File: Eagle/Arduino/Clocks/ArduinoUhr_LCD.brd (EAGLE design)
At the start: 100 x 80 mm, 13 parts

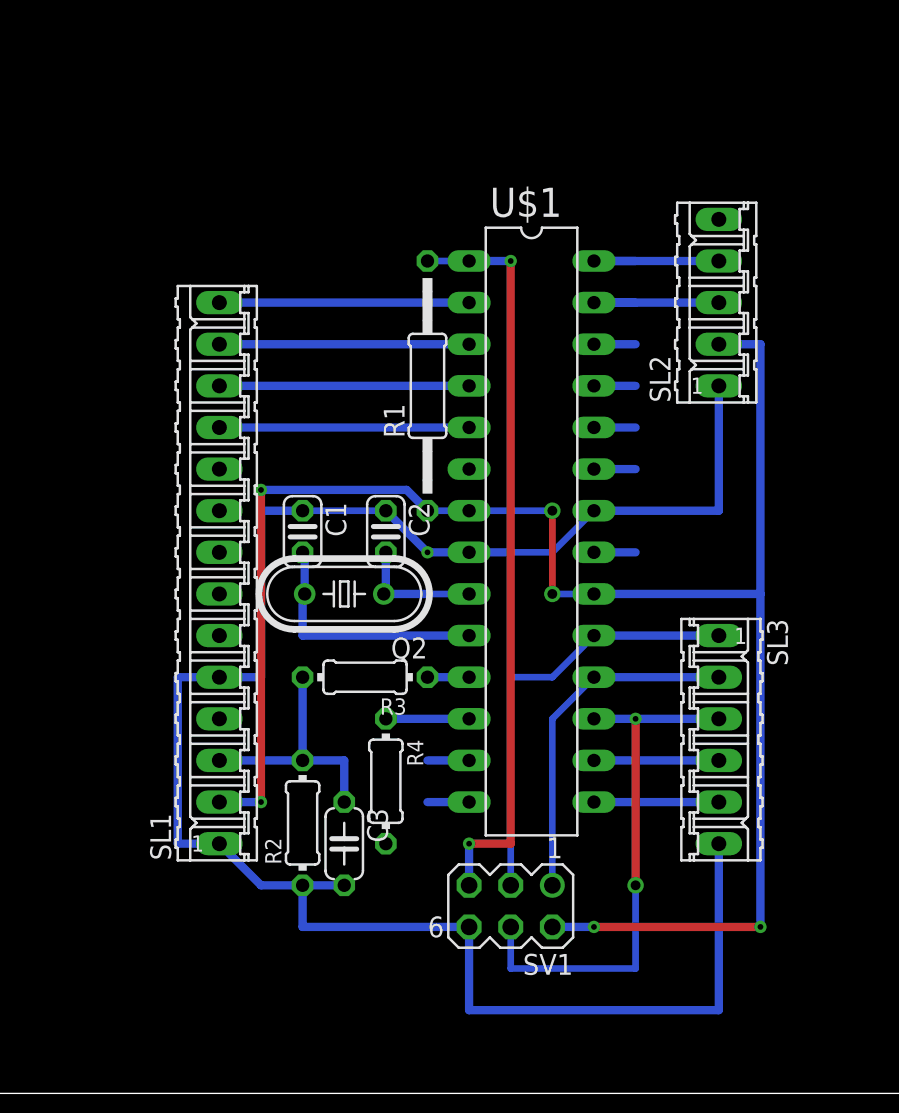
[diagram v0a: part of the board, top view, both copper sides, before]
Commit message: changed layout for new LCD Display
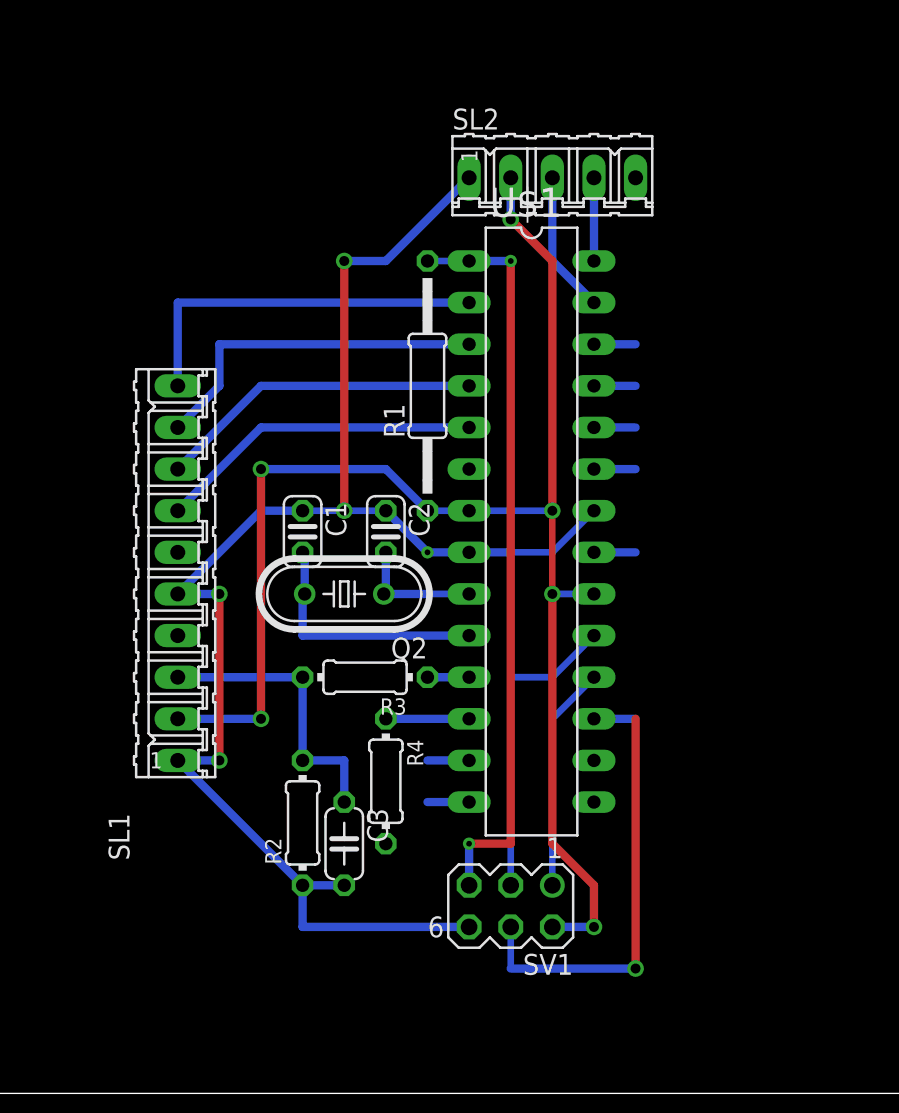
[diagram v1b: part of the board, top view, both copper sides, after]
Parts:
- removed SL3: (no value), con-amp-quick:06P
- SL1: device con-amp-quick:14P -> con-amp-quick:10P
- moved SL2 12.7 mm to (48.3, 55.9), turned to 0 degrees
- moved SL1 2.54 mm to (25.4, 31.8)
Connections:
- removed net D0: SL1.11, U$1.5
- removed net D1: SL1.12, U$1.4
- removed net D2: SL1.13, U$1.3
- removed net D3: SL1.14, U$1.2
- new net N$1: SL1.10, U$1.2
- new net N$2: SL1.9, U$1.3
- new net N$3: SL1.8, U$1.4
- new net N$4: SL1.7, U$1.5
- net DIO10(PWM): no longer SL3.4
- net DIO11(PWM)MOSI: no longer SL3.3
- net DIO12/MISO: no longer SL3.2
- net DIO9(PWM): no longer SL3.5
- net GND: no longer SL3.6
- net SCK[L5]: no longer SL3.1
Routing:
- net N$1: track 0.00 -> 22.9 mm
- net GND: track 117.5 -> 95.8 mm, vias 2 -> 6
- net N$2: track 0.00 -> 21.4 mm
- net N$4: track 0.00 -> 19.9 mm
- net N$3: track 0.00 -> 19.9 mm
- net VCC: track 108.5 -> 92.1 mm
- net D3: track 15.2 -> 0.00 mm
- net D2: track 15.2 -> 0.00 mm
- net D1: track 15.2 -> 0.00 mm
- net D0: track 15.2 -> 0.00 mm
- net SCK[L5]: track 26.5 -> 18.8 mm
- net DIO9(PWM): track 7.62 -> 0.00 mm
- net DIO12/MISO: track 21.4 -> 13.8 mm
- net DIO10(PWM): track 7.62 -> 0.00 mm
- net A5[SCL]: track 10.2 -> 5.08 mm
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
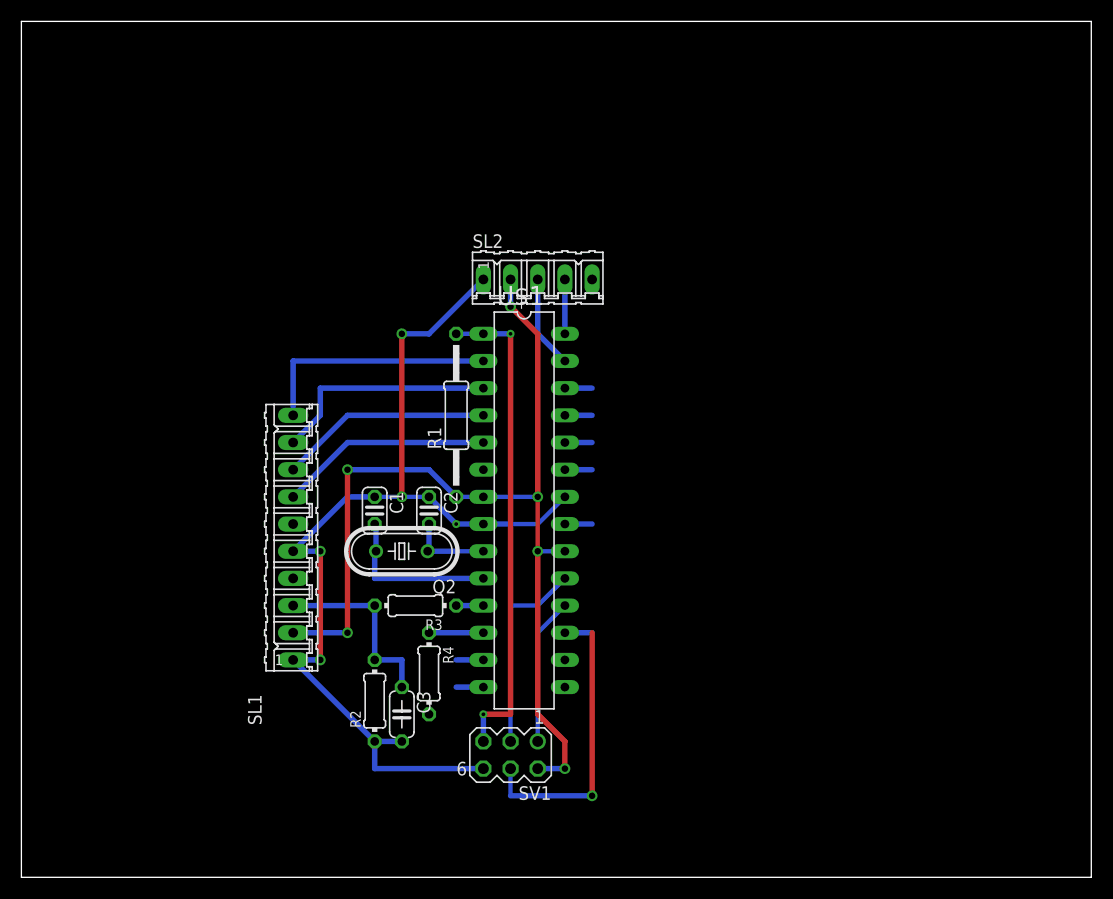
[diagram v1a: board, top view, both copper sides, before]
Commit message: Changes for severals files
bugfixes, pins changed
 - Arduino/Sketches/Uhren/ClockWithTimers/clockwithtimers/SettingStates.cpp
 - Arduino/Sketches/Uhren/ClockWithTimers/clockwithtimers/big_ben.h
 - Arduino/Sketches/Uhren/ClockWithTimers/clockwithtimers/clockwithtimers.ino
 - Arduino/Sketches/Uhren/ClockWithTimers/clockwithtimers/ioAt328.h
 - Arduino/Sketches/Uhren/ClockWithTimers/clockwithtimers/ioMega2560.h
bugfixes, and comments
 - Arduino/libraries/Melody/examples/melody_play/melody_play.ino
 - Arduino/libraries/Melody/keywords.txt
 - Arduino/libraries/Melody/library.properties
 - Arduino/libraries/Melody/src/Melody.h
Layout for arduino pins changed
 - Eagle/Arduino/Clocks/ArduinoUhr_LCD.brd
 - Eagle/Arduino/Clocks/ArduinoUhr_LCD.sch
Added a thread for arduino loop
 - Qt/ArduinoUnittest/ArduinoUnittest/ArduinoUnittest.pro
 - Qt/ArduinoUnittest/ArduinoUnittest/arduinoworker.cpp
 - Qt/ArduinoUnittest/ArduinoUnittest/arduinoworker.h
 - Qt/ArduinoUnittest/ArduinoUnittest/mainwindow.cpp
 - Qt/ArduinoUnittest/ArduinoUnittest/mainwindow.h
bugfix
 - Qt/SerialCommunicator/SerialCommunicator/mainwindow.cpp
 - Qt/SerialCommunicator/SerialCommunicator/pincommon.h
c++17 fallthrough for code clarity
 - Qt/acalc/src/acalc.pro
 - Qt/acalc/src/carithmetic.cpp
 - Qt/acalc/src/carithmetic.h
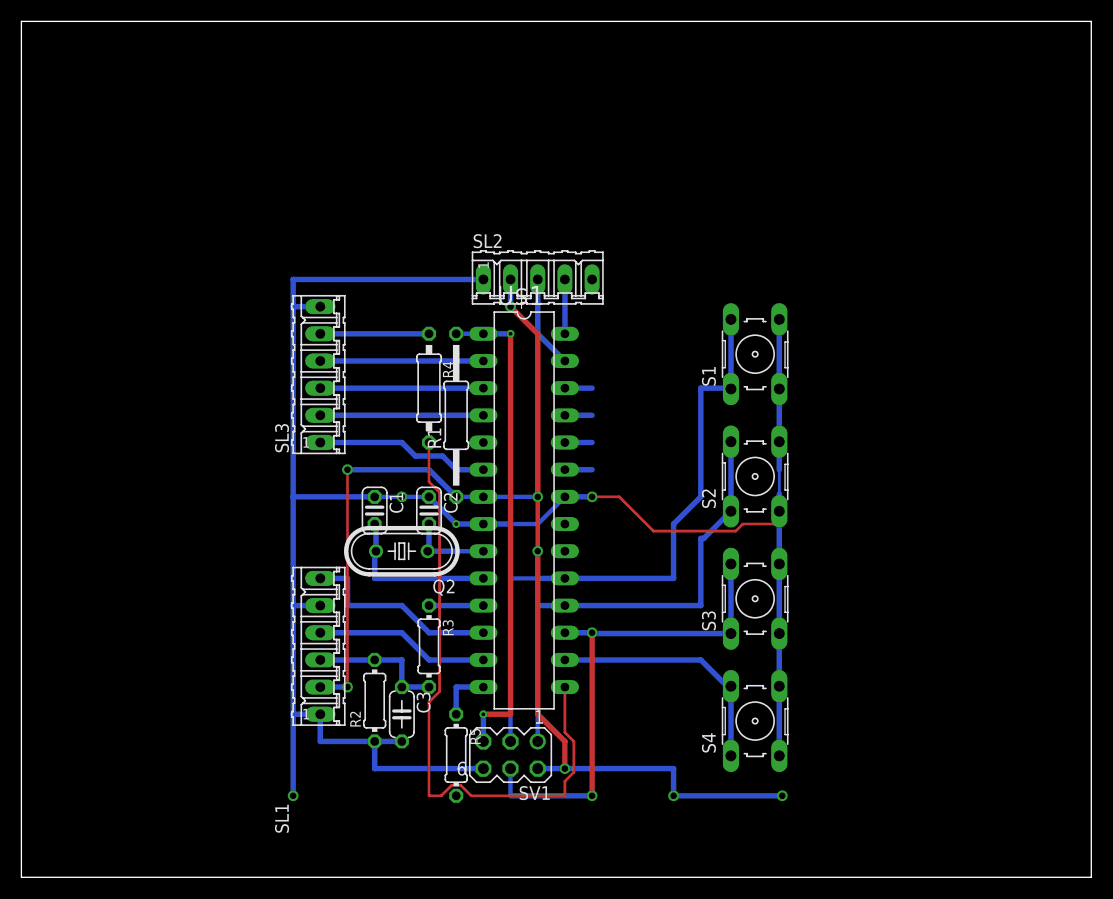
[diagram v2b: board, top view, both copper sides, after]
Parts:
- added R5: 150, rcl:0204/7
- added S1, S2, S3, S4: (no value), switch-omron:B3F-10XX
- added SL3: (no value), con-amp-quick:06P
- C3: value (none) -> 1µF
- R2: value (none) -> 1k
- R3: value (none) -> 2k2
- R4: value (none) -> 150; device rcl:0204/7 -> resistor:0207/10
- SL1: device con-amp-quick:10P -> con-amp-quick:06P
- moved R4 26.7 mm to (38.1, 45.7)
- moved SL1 10.5 mm to (27.9, 21.6)
- moved R3 4.02 mm to (38.1, 21.6), turned to 270 degrees
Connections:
- net DIO5(PWM)[RS] renamed DIO5(PWM)
- removed net AREF: U$1.21
- removed net DIO10(PWM): U$1.16
- removed net DIO11(PWM)MOSI: SV1.4, U$1.17
- removed net DIO12/MISO: SV1.1, U$1.18
- removed net DIO4[ENABLE]: U$1.6
- removed net DIO6(PWM)[TONE]: R4.1, U$1.12
- removed net DIO7[SWITCH1]: U$1.13
- removed net DIO8[SWITCHT2]: U$1.14
- removed net DIO9(PWM): U$1.15
- removed net ENABLE: SL1.6
- removed net LED_LIGHT: R4.2
- removed net N$1: SL1.10, U$1.2
- removed net N$4: SL1.7, U$1.5
- removed net RS: SL1.4
- removed net SCK[L5]: SV1.3, U$1.19
- new net D0: SL3.4, U$1.2
- new net D1: SL3.3, U$1.3
- new net D2: SL3.2, U$1.4
- new net D4: SL3.1, U$1.6
- new net D6[ENABLE]: SL1.6, U$1.12
- new net D7[RS]: SL1.4, U$1.13
- new net DIO10(PWM)[SW1]: S4.1, S4.2, U$1.16
- new net DIO11(PWM)MOSI[SW2]: S3.1, S3.2, SV1.4, U$1.17
- new net DIO12/MISO[SW3]: S2.1, S2.2, SV1.1, U$1.18
- new net DIO8[TONE]: R5.1, U$1.14
- new net DIO9(PWM)[LED]: R4.2, U$1.15
- new net SCK[SW4]: S1.1, S1.2, SV1.3, U$1.19
- net GND: now also S1.3, S1.4, S2.3, S2.4, S3.3, S3.4, S4.3, S4.4, SL3.6
- net N$2: now also R4.1, SL3.5; no longer SL1.9, U$1.3
- net N$3: now also R5.2; no longer SL1.8, U$1.4
- net VCC: no longer U$1.20
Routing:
- net GND: track 95.8 -> 188.0 mm
- net SCK[SW4]: track 0.00 -> 58.6 mm
- net DIO9(PWM)[LED]: track 0.00 -> 58.2 mm
- net DIO11(PWM)MOSI[SW2]: track 0.00 -> 47.6 mm, vias 0 -> 2
- net DIO12/MISO[SW3]: track 0.00 -> 44.6 mm
- net DIO11(PWM)MOSI: track 27.9 -> 0.00 mm, vias 1 -> 0
- net DIO10(PWM)[SW1]: track 0.00 -> 23.0 mm
- net VCC: track 92.1 -> 114.9 mm, vias 6 -> 8
- net N$1: track 22.9 -> 0.00 mm
- net N$4: track 19.9 -> 0.00 mm
- net N$3: track 19.9 -> 0.00 mm
- net SCK[L5]: track 18.8 -> 0.00 mm
- net D6[ENABLE]: track 0.00 -> 18.8 mm
- net D7[RS]: track 0.00 -> 16.3 mm
- net D4: track 0.00 -> 16.3 mm
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
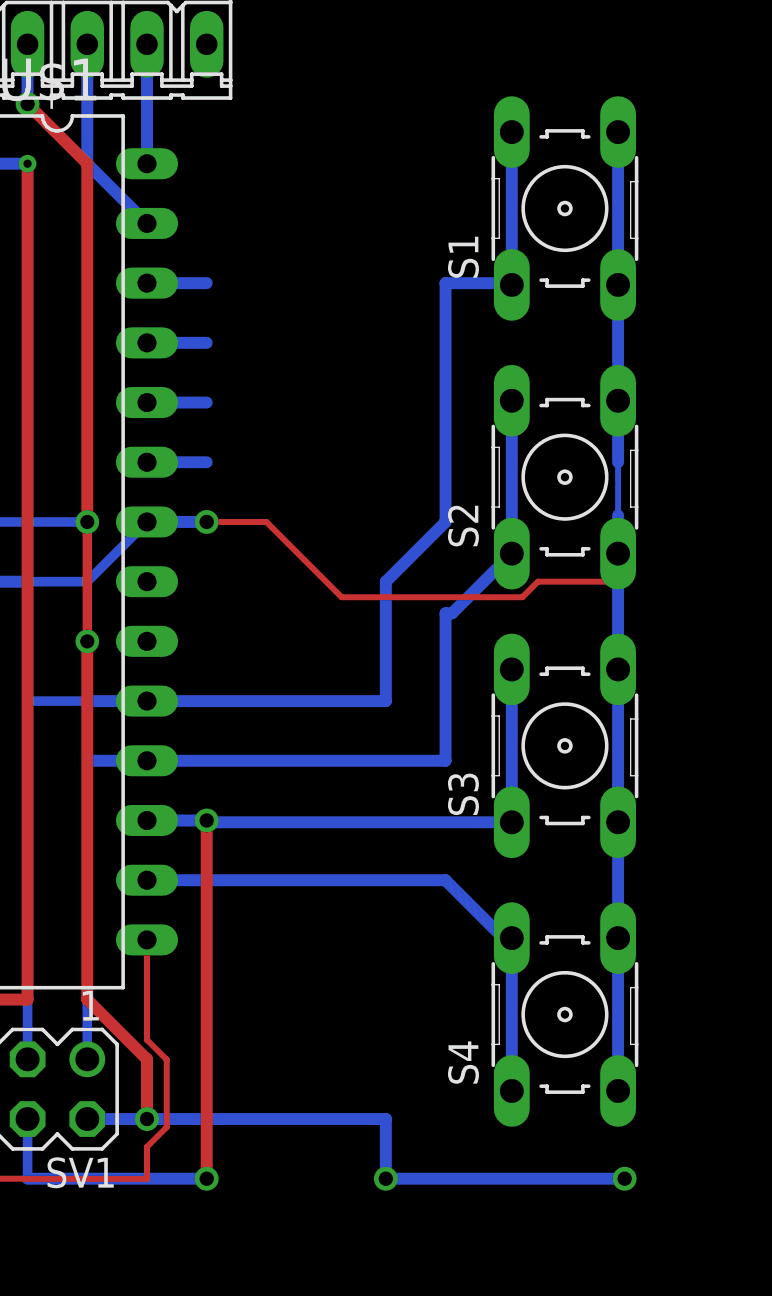
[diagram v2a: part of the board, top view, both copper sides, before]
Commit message: added language selection and usb current measurement
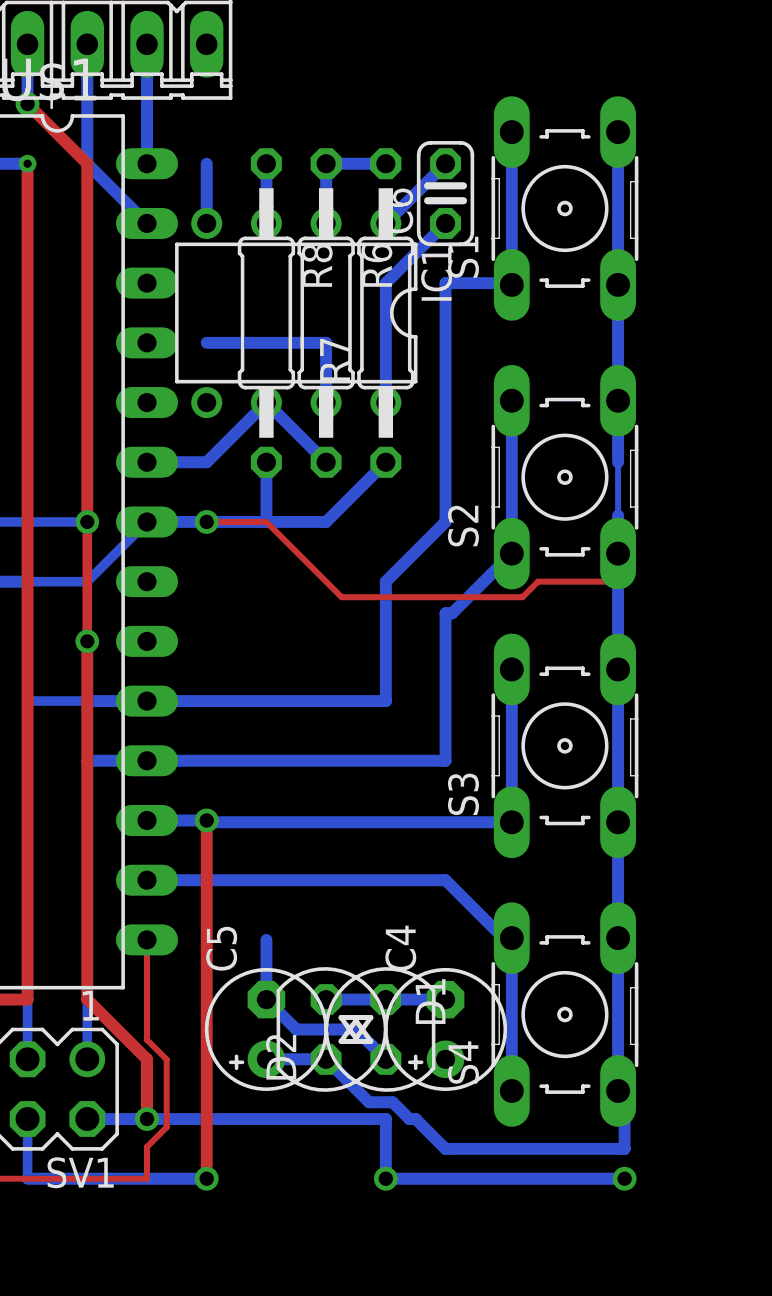
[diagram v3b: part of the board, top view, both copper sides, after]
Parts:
- added C4, C5: (no value), rcl:E2,5-5
- added C6: (no value), rcl:C025-024X044
- added D1, D2: BB112, diode:SOT54H
- added IC1: UA748P, linear:DIL08
- added R6: 22k, rcl:0207/12
- added R7: 2k2, rcl:0207/12
- added R8: R62, rcl:0207/12
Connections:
- removed net A0[BATTERY]: U$1.23
- new net A0[CURRENT]: IC1.6, R6.2, U$1.23
- new net COMP: C6.1, IC1.8
- new net D3: C4.+, U$1.5
- new net N$1: C4.-, D1.C, D2.A
- new net N$4: C6.2, IC1.1
- new net N$5: IC1.2, R6.1, R7.2
- new net N2: IC1.5
- new net OUT_GND: IC1.3, R8.1
- new net VDD: C5.-, D1.A, IC1.4
- net GND: now also C5.+, D2.C, R7.1, R8.2
- net VCC: now also IC1.7
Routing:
- net GND: track 188.0 -> 218.7 mm
- net VDD: track 0.00 -> 11.2 mm
- net A0[CURRENT]: track 0.00 -> 9.72 mm
- net COMP: track 0.00 -> 8.67 mm
- net VCC: track 114.9 -> 122.5 mm
- net N$5: track 0.00 -> 5.08 mm
- net N$1: track 0.00 -> 5.08 mm
- net N$4: track 0.00 -> 3.59 mm
- net A3: track 2.54 -> 0.00 mm
- net A2: track 2.54 -> 0.00 mm
- net A1[TEMPERATURE]: track 2.54 -> 0.00 mm
- net A0[BATTERY]: track 2.54 -> 0.00 mm
- net OUT_GND: track 0.00 -> 2.54 mm
